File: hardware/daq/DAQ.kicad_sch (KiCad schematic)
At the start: 141 parts, among them J1 ICD15S13E4GX00LF, J2 ICD15S13E4GX00LF, J3 ICD15S13E4GX00LF, P1 0022272021, U1 ADS124S08IRHBT, U2 ADS124S08IRHBT, U3 LT6654BMPS6-5-TRMPBF, U4 LM1086IS-5.0_NOPB, U5 TPS73801DCQR, U6 TPSM63603RDHR, U7 TPSM63603RDHR, U8 TPSM63603RDHR

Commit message: added an ADC to schematic and started absolutely destroying the layout
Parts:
- added C75, C76, C77, C78: 16nF, GRM3195C2A163JA01D:CAPC3216X95N, symbol Device:C
- added C87, C88, C93: 10uF, GRM21BC71E106KE11L:CAPC2012X145N, symbol Device:C
- added C89, C90, C94: 1uF, 0603YC105JAT2A:CAPC1608X94N, symbol Device:C
- added C91, C92, C95: 100nF, VJ0603Y104JXXAC:CAPC1608X97N, symbol Device:C
- added R45, R46, R47, R48: 10k, footprints10kR:RC0603N_YAG-M, symbol Device:R
- added U9: ADS124S08IRHBT, footprintsADC:RHB0032M, symbol 2025-01-27_01-32-37:ADS124S08IRHBT
- RP1: value Raspberry_Pi_5 -> Raspberry_Pi_4; Description_1 Raspberry Pi Zero 2 or 3 Single-board Computers -> (none)
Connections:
- net +3.3V: now also C93.1, C94.1, C95.1, U9.15 (IOVDD), U9.16 (DVDD)
- net +5Vs: now also C88.1, C90.1, C92.1, U9.26 (AVDD)
- net 5V REF: now also C87.2, C89.2, C91.2, U9.30 (REFP0)
- net GND: now also C75.2, C76.2, C77.2, C78.2, C87.1, C88.2, C89.1, C90.2, C91.1, C92.2, C93.2, C94.2, C95.2, U9.1 (AINCOM), U9.14 (DGND), U9.17 (CLK), U9.24 (REFCOM), U9.27 (AVSS), U9.28 (AVSS), U9.29 (REFN0), U9.33 (PAD)
- net MISO: now also U9.12 (DOUT_DRDY_N)
- net MOSI: now also U9.10 (DIN)
- net SCLK: now also U9.11 (SCLK)
- new net: C78.1, R48.2, U9.20 (GPIO2_AIN10)
- new net: C76.1, R46.2, U9.7 (AIN0)
- new net: C77.1, R47.2, U9.19 (GPIO3_AIN11)
- new net: C75.1, R45.2, U9.6 (AIN1)
- new net CE3: U9.9 (CS_N)
- new net DRDY_N3: U9.13 (DRDY_N)
- new net IDAC1_3: U9.2 (AIN5)
- new net IDAC2_3: U9.4 (AIN3)
- new net PT10_SIG: R48.1
- new net PT7_SIG: R45.1
- new net PT8_SIG: R46.1
- new net PT9_SIG: R47.1
- new net RESET_N3: U9.18 (RESET_N)
- new net START_SYNC3: U9.8 (START_SYNC)
- no-connect marks 36 -> 38
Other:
- note added: "***maybe drop 10Vs to 9Vs or 9.5Vs"
- note added: "11V to LDO -> 10V for Load Cell Excitation"
- note added: "5V for ADC AVDD"
- note added: "5V supply for Pi"
- note added: "6V to LDO -> 5V for ADC AVDD"
- note added: "Clean 10V for load cell excitation"
- note added: "Low Dropout Regulator"
- note added: "Precision 5V Reference for ADC"
- note added: "Precision Reference IC"
- note added: "TOTAL SENSOR CAPABILITIES: - 10 PTs - 2 RTDs - 3 Load Cells"
- note added: "should replace these w/ 26 position D-SUBs"
- note removed: "LOW DROPOUT REGULATORS"
- moved on the sheet: C1, C10, C11, C14, C15, C16, C17, C18, C2, C21, C22, C23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

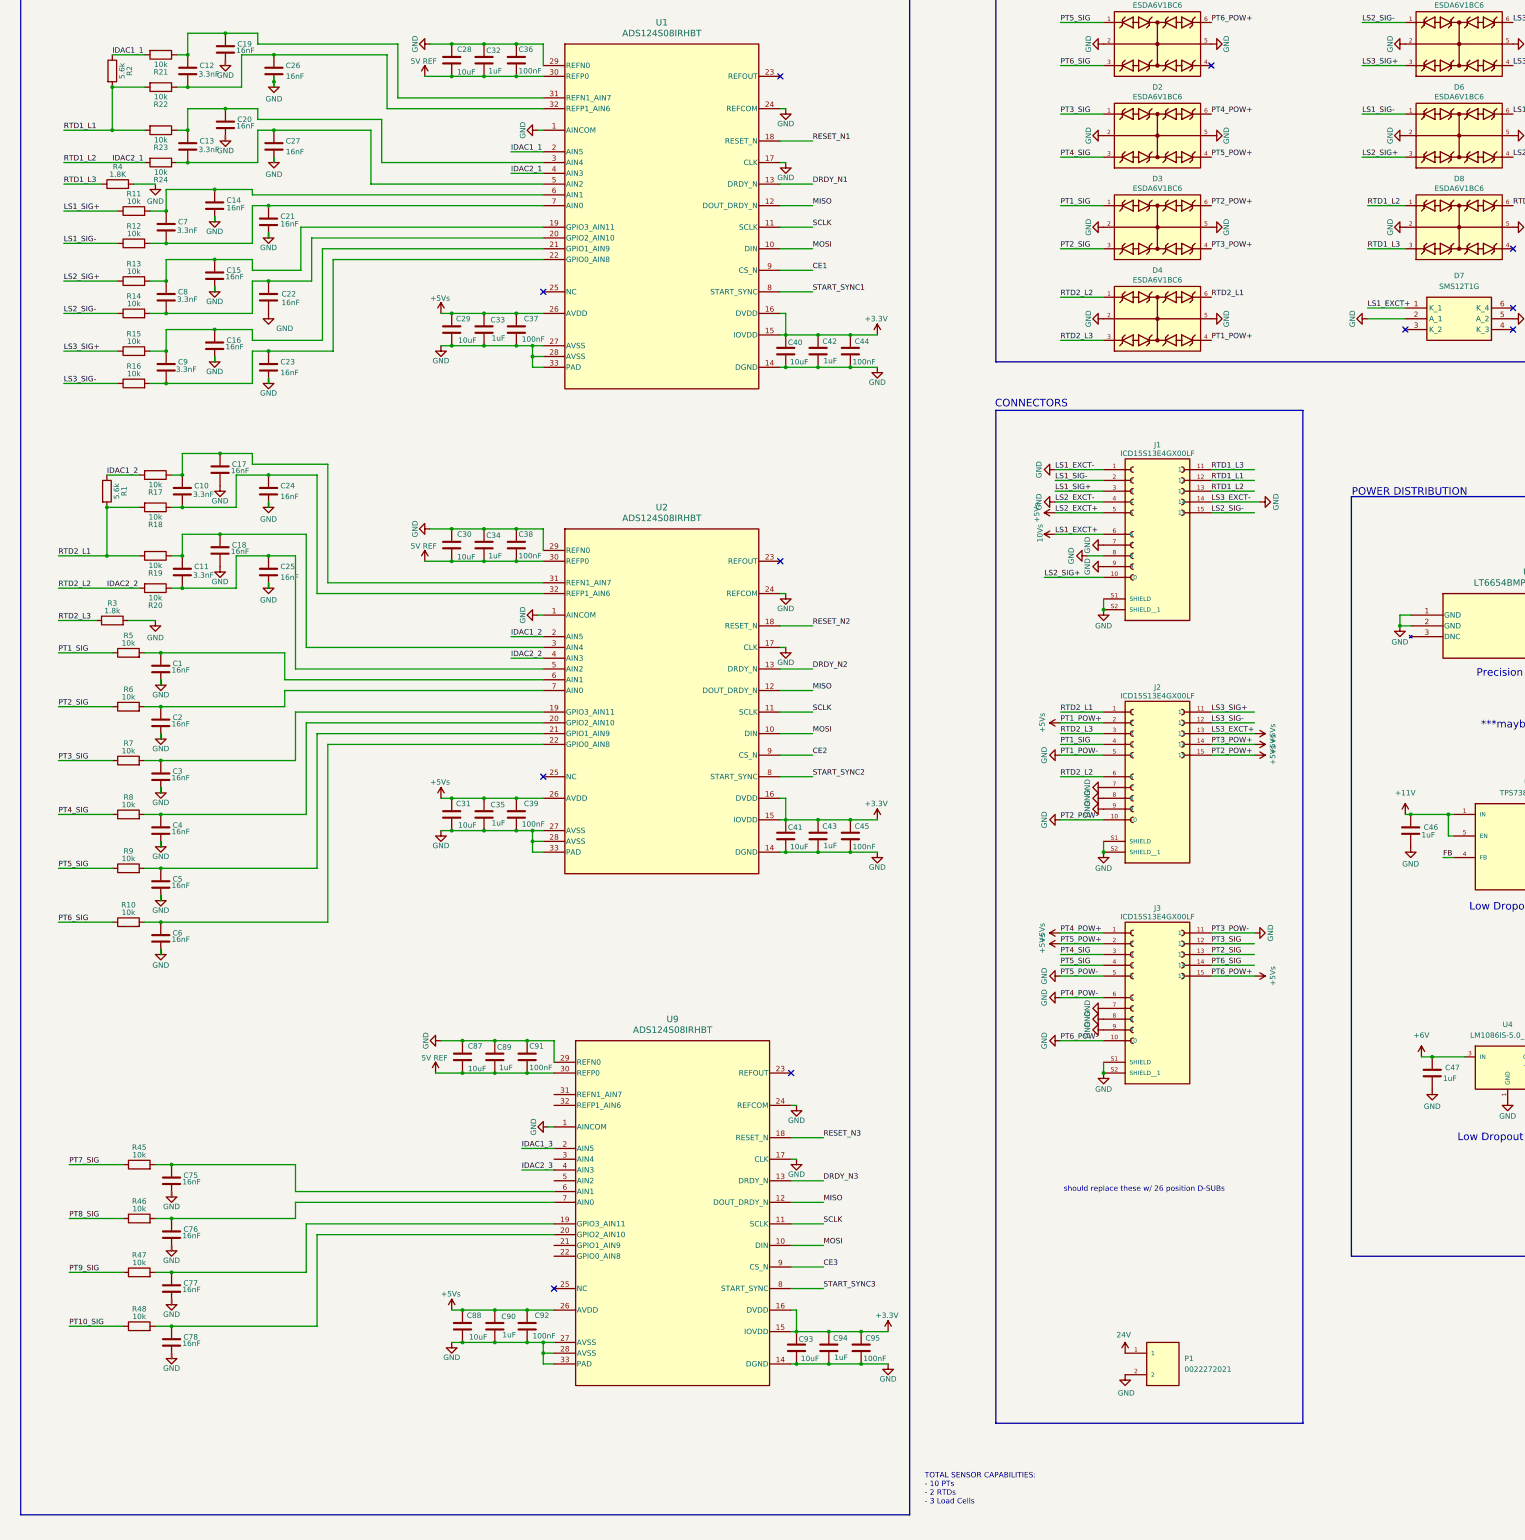
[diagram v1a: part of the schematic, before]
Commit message: checking out 26pin, having footprint library issues yay
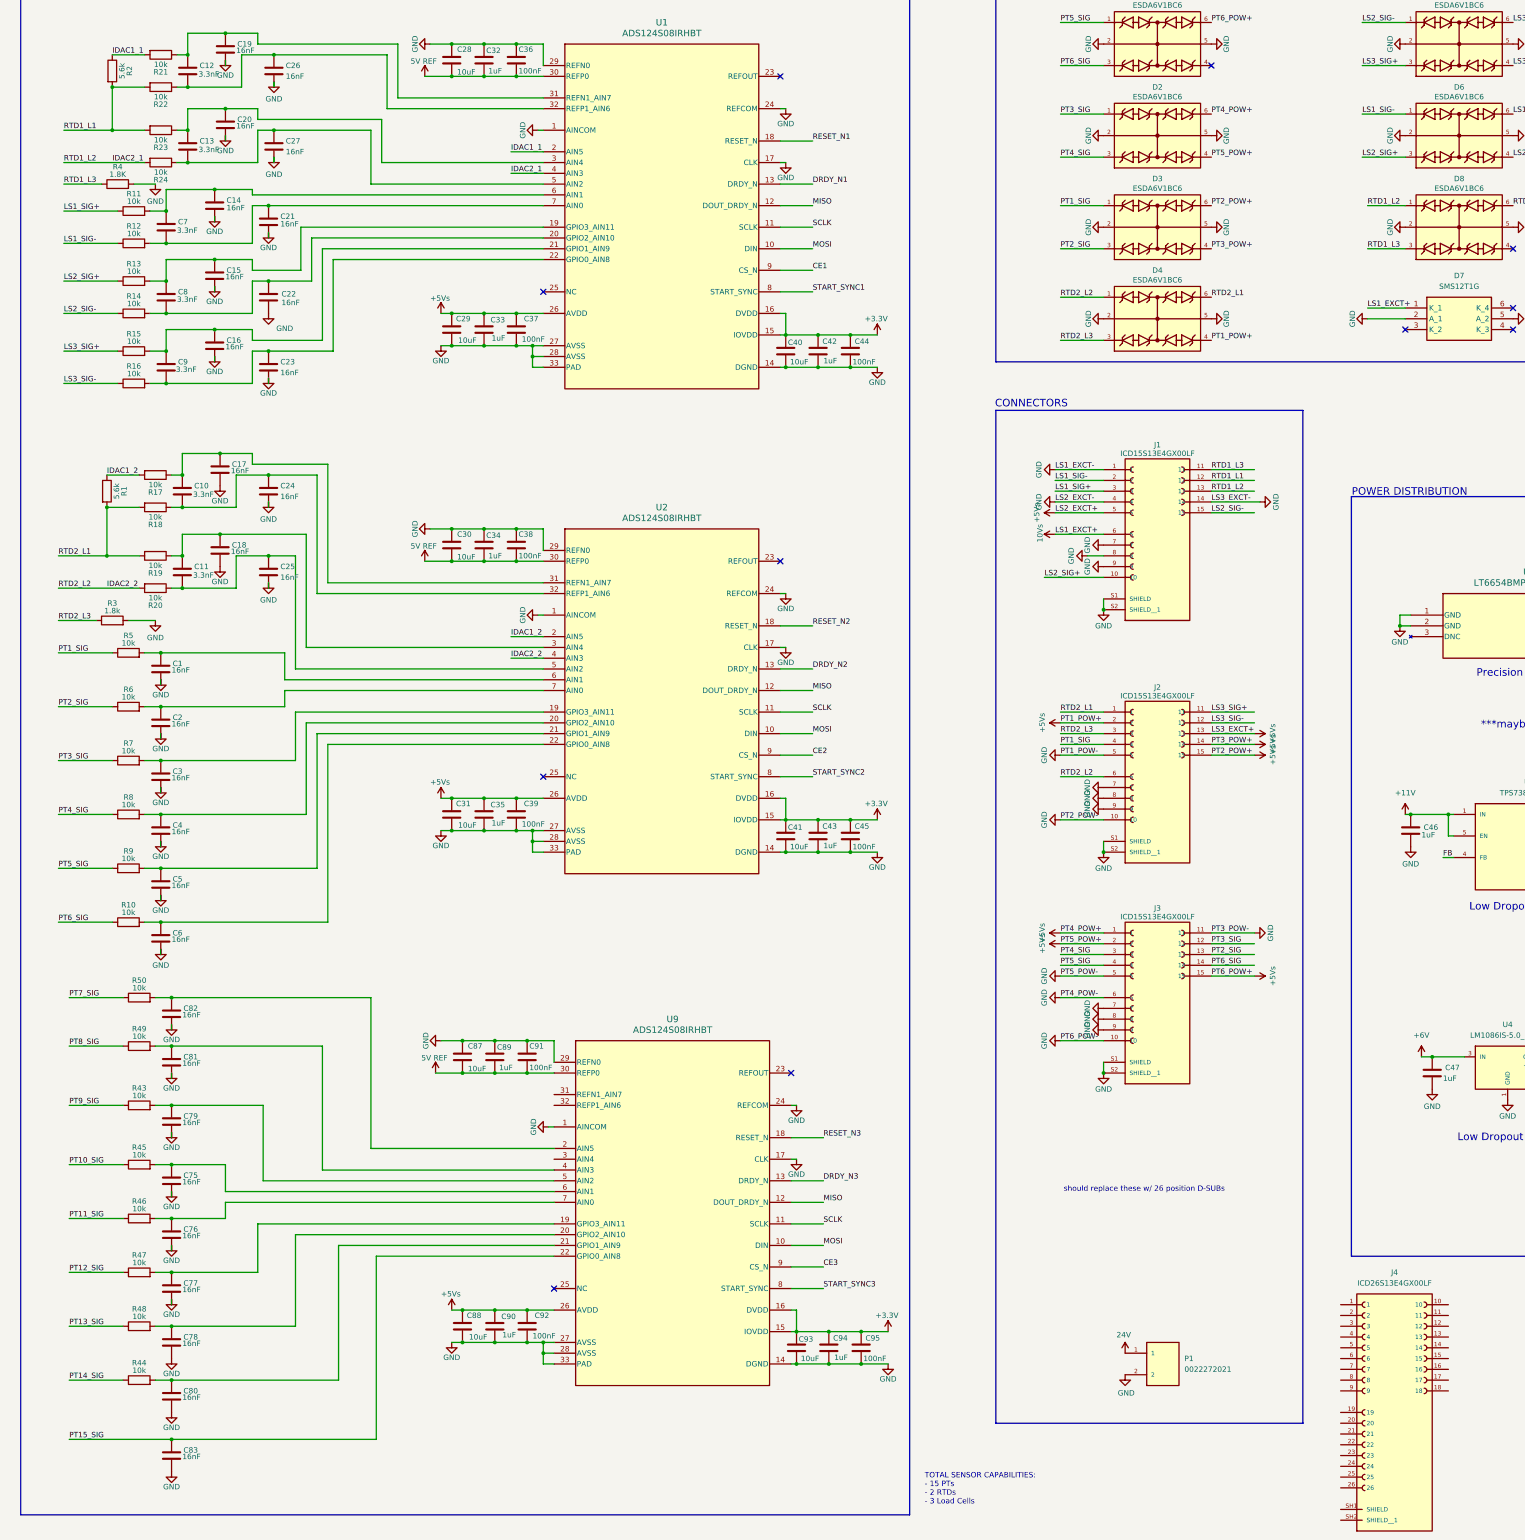
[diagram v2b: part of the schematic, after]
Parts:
- added C79, C80, C81, C82, C83: 16nF, GRM3195C2A163JA01D:CAPC3216X95N, symbol Device:C
- added J4: ICD26S13E4GX00LF, ICD26S13E4GX00LF:AMPHENOL_ICD26S13E4GX00LF, symbol Connector:ICD26S13E4GX00LF
- added R43, R44, R49, R50: 10k, footprints10kR:RC0603N_YAG-M, symbol Device:R
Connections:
- net GND: now also C79.2, C80.2, C81.2, C82.2, C83.2
- net PT10_SIG: now also R45.1; no longer R48.1
- net PT7_SIG: now also R50.1; no longer R45.1
- net PT8_SIG: now also R49.1; no longer R46.1
- net PT9_SIG: now also R43.1; no longer R47.1
- net at U9.21 (GPIO1_AIN9): now also C80.1, R44.2
- net PT15_SIG: now reaches U9.22 (GPIO0_AIN8)
- net PT15_SIG: now also C83.1
- net at U9.5 (AIN2): now also C79.1, R43.2
- net IDAC1_3: no longer names the net of U9.2 (AIN5)
- net IDAC1_3: now also C82.1, R50.2
- net IDAC2_3: no longer names the net of U9.4 (AIN3)
- net IDAC2_3: now also C81.1, R49.2
- new net PT11_SIG: R46.1
- new net PT12_SIG: R47.1
- new net PT13_SIG: R48.1
- new net PT14_SIG: R44.1
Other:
- note added: "TOTAL SENSOR CAPABILITIES: - 15 PTs - 2 RTDs - 3 Load Cells"
- note removed: "TOTAL SENSOR CAPABILITIES: - 10 PTs - 2 RTDs - 3 Load Cells"
